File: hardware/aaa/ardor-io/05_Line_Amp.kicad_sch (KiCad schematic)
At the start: 18 parts, among them J501 LINE OUT / 6.3mm TS, J502 TO YOUR AMP CIRCUIT, J503 TO LINE PANEL / T,S, K501 G5V-1 DC5, Q501 2N7002, U501 OPA2320AIDR

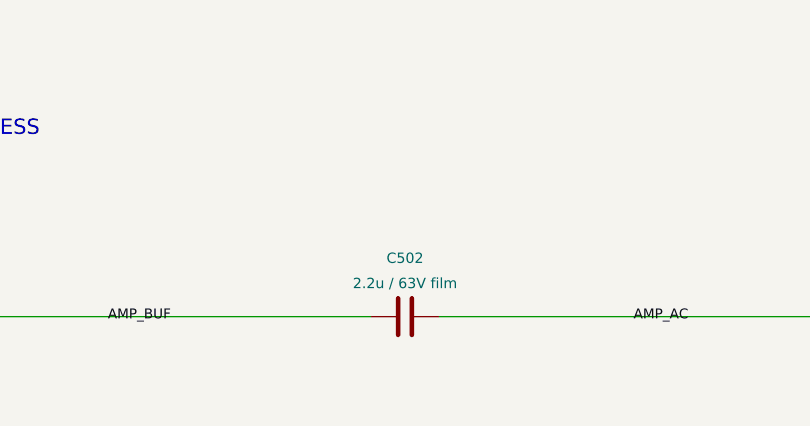
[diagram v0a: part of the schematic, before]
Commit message: feat: smd capacitors
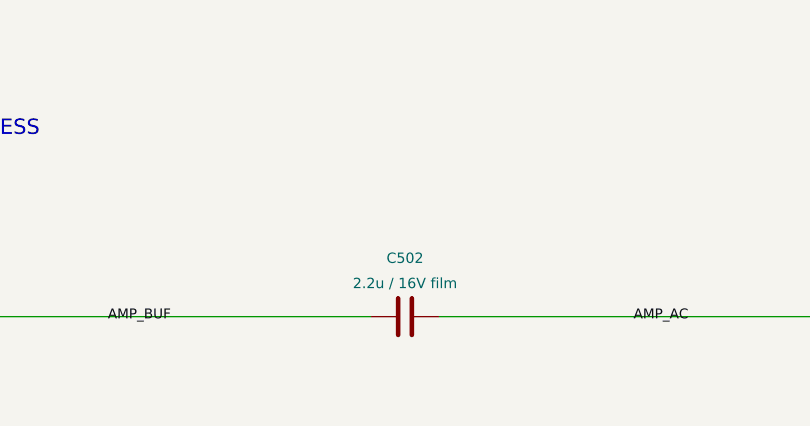
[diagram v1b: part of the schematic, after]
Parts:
- C502: value 2.2u / 63V film -> 2.2u / 16V film; footprint Capacitor_THT:C_Rect_L7.2mm_W7.2mm_P5.00mm_FKS2_FKP2_MKS2_MKP2 -> Ardor_Capacitor:C_Rubycon_MU_3225; MPN WIMA MKS2C042201K00KSSD -> Rubycon 16MU225KB23225

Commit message: feat: update Ardor IO PCB for hardware rev2
- Update schematics, routing, BOM, and design documentation
- Add SMD capacitor conversion and verification tooling
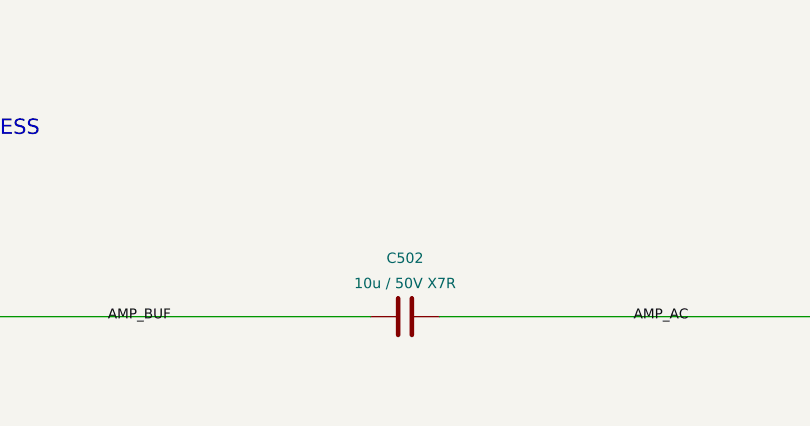
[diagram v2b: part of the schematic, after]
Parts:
- C502: value 2.2u / 16V film -> 10u / 50V X7R; footprint Ardor_Capacitor:C_Rubycon_MU_3225 -> Capacitor_SMD:C_1206_3216Metric; JLCPCB Part # (none) -> C89632; MPN Rubycon 16MU225KB23225 -> Samsung CL31B106KBHNNNE

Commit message: feat: finalize Ardor IO hardware rev2 production package
- Update schematics, PCB, BOM, and documentation
- Add assembly exports, review artifacts, and verification data
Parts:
- C501: footprint Capacitor_SMD:CP_Elec_6.3x5.4 -> Ardor_Capacitor:CP_Elec_Panasonic_FK_D6.3_H5.8; JLCPCB Part # (none) -> C336261; MPN Panasonic EEE-FK1C470R -> Panasonic EEEFK1C470P
- C503: value 100n / 16V -> 100n / 50V X7R; JLCPCB Part # (none) -> C14663; MPN (none) -> YAGEO CC0603KRX7R9BB104
- D501: JLCPCB Part # (none) -> C19224; MPN Nexperia PESD5V0S1BA -> Nexperia PESD5V0S1BA,115
- D502: JLCPCB Part # (none) -> C81598; MPN 1N4148W -> ST(Semtech) 1N4148W
- Q501: value 2N7002 -> AO3400A; symbol Ardor:2N7002 -> Ardor:AO3400A; JLCPCB Part # (none) -> C20917; MPN Nexperia 2N7002 -> Alpha & Omega AO3400A
- R501: JLCPCB Part # (none) -> C25804; MPN (none) -> UNI-ROYAL 0603WAF1002T5E
- R502: JLCPCB Part # (none) -> C22775; MPN (none) -> UNI-ROYAL 0603WAF1000T5E
- R503, R505: JLCPCB Part # (none) -> C21190; MPN (none) -> UNI-ROYAL 0603WAF1001T5E
- R504, R506: JLCPCB Part # (none) -> C25803; MPN (none) -> UNI-ROYAL 0603WAF1003T5E
- U501: JLCPCB Part # (none) -> C2863402
